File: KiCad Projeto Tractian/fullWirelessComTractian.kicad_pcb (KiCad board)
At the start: 4 copper layers, 23 parts, among them U1 ESP8266EX, U2 MX25R3235FM2xx1, U4 MX25R3235FM2xx1, U5 AMS1117-3.3, Y2 XTAL

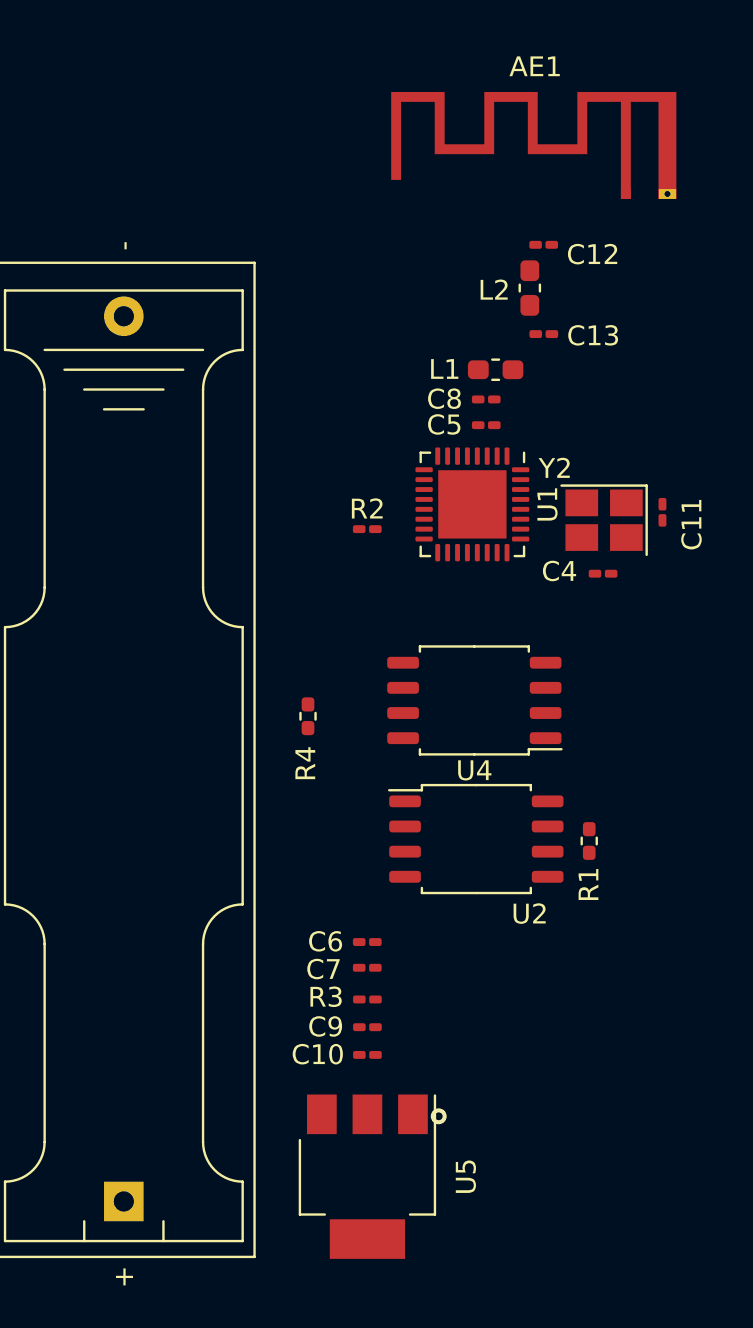
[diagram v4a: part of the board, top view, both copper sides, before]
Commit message: :construction: Schematics reorganizado | definicao de trail mils para power/GND lines e signal lines
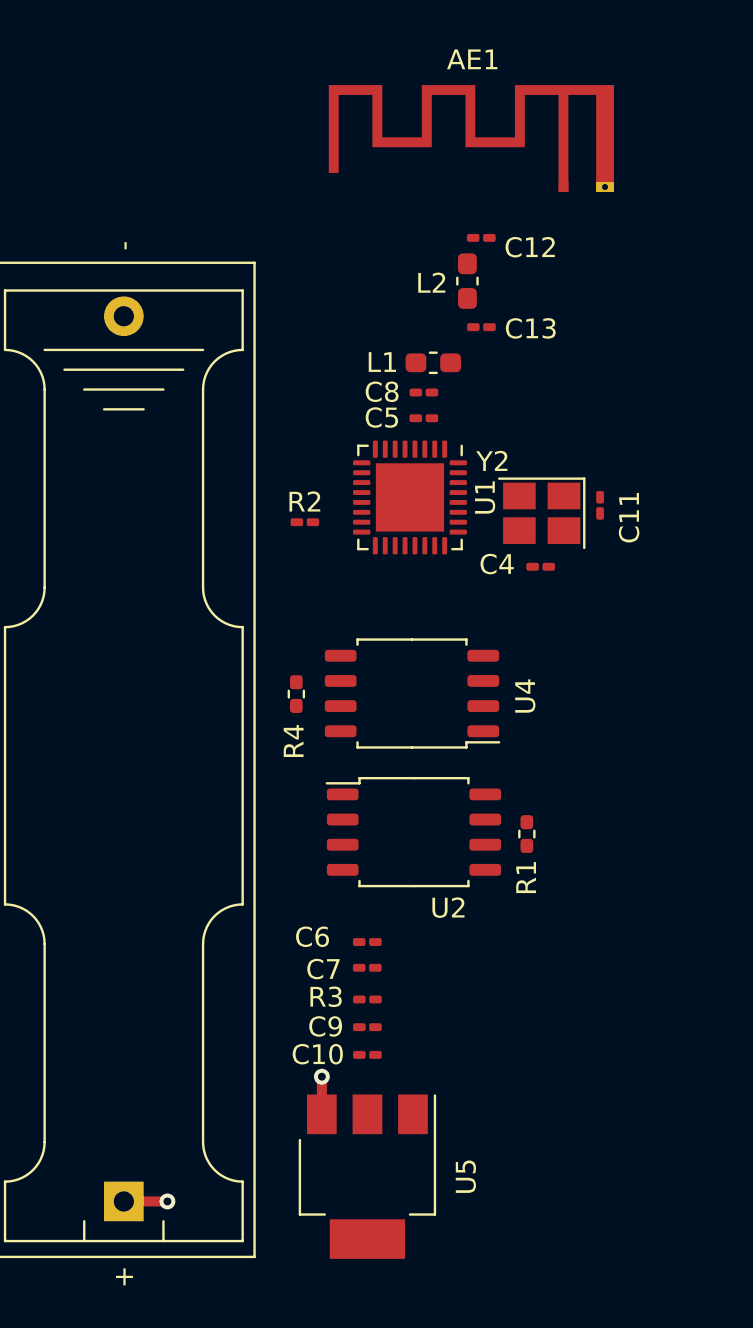
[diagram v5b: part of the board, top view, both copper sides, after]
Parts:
- Y2: value XTAL -> XTAL 16Mhz ±10ppm (TSX -3225 )
- moved AE1 3.17 mm to (149.5, 68.0)
- moved C11 3.17 mm to (151.3, 84.0)
- moved C13 3.17 mm to (145.4, 75.0)
- moved C8 3.17 mm to (142.4, 78.3)
- moved L2 3.17 mm to (144.7, 72.7)
- moved R1 3.17 mm to (147.7, 100.6)
- moved U2 3.17 mm to (141.9, 100.5)
- moved U4 3.17 mm to (141.8, 93.5)
- moved C12 3.17 mm to (145.3, 70.5)
- moved C4 3.17 mm to (148.3, 87.2)
- moved C5 3.17 mm to (142.4, 79.7)
- moved R2 3.17 mm to (136.4, 84.9)
- moved U1 3.17 mm to (141.8, 83.7)
- moved Y2 3.17 mm to (148.4, 84.5)
- moved L1 3.17 mm to (142.9, 76.8)
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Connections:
- net Net-(U1-VDDD) renamed VDD33
- net Net-(U2-SCLK) renamed DMSCK
- U1 pad 12: Net-(U1-MTCK) -> unconnected-(U1-MTCK-Pad12)
- U1 pad 14: Net-(U1-GPIO2) -> DMH
- U1 pad 15: Net-(U1-GPIO0) -> DMW
- U2 pad 3: Net-(U1-GPIO0) -> DMWP
- U2 pad 5: Net-(U1-MTCK) -> DMSI
- U2 pad 7: Net-(U1-GPIO2) -> DMHD
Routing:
- net Net-(BT1-+): track 0.00 -> 14.5 mm, vias 0 -> 2
- net (no net): vias 1 -> 0

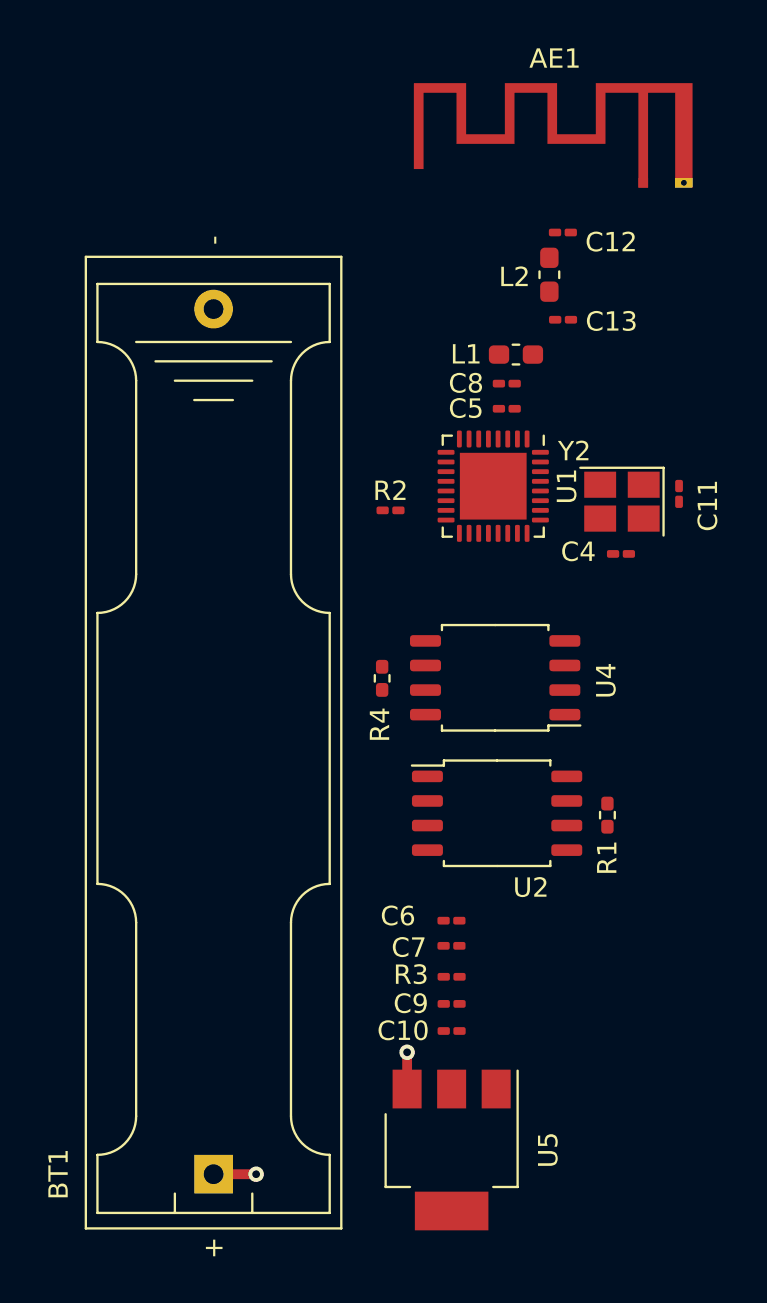
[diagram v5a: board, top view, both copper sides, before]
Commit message: 1 - :boom: | 2 - :memo: | 1- Calculo e projeto da impedancia de 50ohms para a antena RF | 2 - add datasheet antena RTexasSWRA117D 2.4GHz
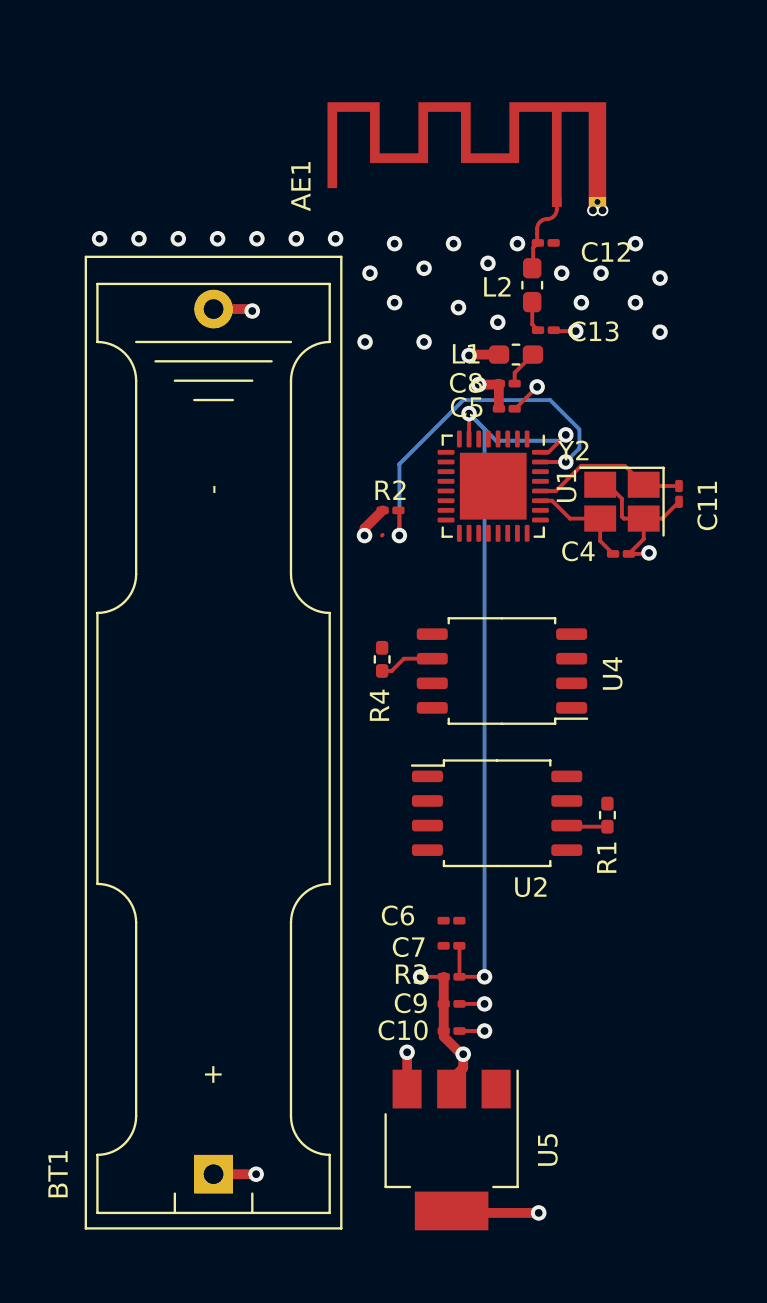
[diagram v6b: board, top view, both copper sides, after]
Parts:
- moved AE1 4.57 mm to (145.0, 69.0)
- moved C13 1.04 mm to (144.5, 75.6)
- moved L2 1.04 mm to (143.8, 73.3)
- moved C12 1.04 mm to (144.5, 71.1)
- moved R4 0.98 mm to (136.0, 92.6)
- moved U4 0.49 mm to (142.2, 93.2)
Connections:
- net DMSCK renamed DMCLK
- net Net-(U1-MTDI) renamed DMSO
- net Net-(U1-MTDO) renamed DMCS
- net Net-(U1-SDIO_CMD) renamed PMCS
- net Net-(U1-SDIO_DATA_0) renamed PMSO
- net Net-(U1-SDIO_DATA_1) renamed PMSI
- net Net-(U1-SDIO_DATA_2) renamed PMHD
- net Net-(U1-SDIO_DATA_3) renamed PMWP
- net Net-(U4-SCLK) renamed PMCLK
- U1 pad 12: unconnected-(U1-MTCK-Pad12) -> DMSI
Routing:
- net VDD33: track 0.00 -> 62.6 mm, vias 0 -> 5
- net Net-(U1-CHIP_PU): track 0.00 -> 41.0 mm, vias 0 -> 3
- net GND: track 0.00 -> 27.6 mm, vias 0 -> 34
- net Net-(U1-RES12K): track 0.00 -> 19.6 mm, vias 0 -> 2
- net Net-(U1-XTAL_IN): track 0.00 -> 8.13 mm
- net Net-(U1-XTAL_OUT): track 0.00 -> 5.57 mm
- net PMCLK: track 0.00 -> 2.85 mm
- net DMCLK: track 0.00 -> 2.12 mm
- net Net-(C8-Pad1): track 0.00 -> 1.89 mm
- net Net-(U1-LNA): track 0.00 -> 1.60 mm
- net Net-(AE1-A): track 0.00 -> 1.43 mm
- added copper zone on In1.Cu, net GND

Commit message: :construction: Nova organizacao da PCB | Routing in progress
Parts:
- added C1: 0.1uF, Capacitor_SMD:C_0201_0603Metric_Pad0.64x0.40mm_HandSolder, F.Cu at (151.4, 113.3)
- added C2: 2.2uF, Capacitor_Tantalum_SMD:CP_EIA-1608-08_AVX-J_Pad1.25x1.05mm_HandSolder, F.Cu at (151.4, 115.3)
- added R5: 220kΩ ±1%, Resistor_SMD:R_0201_0603Metric_Pad0.64x0.40mm_HandSolder, F.Cu at (152.3, 90.7)
- added R6: 100kΩ ±1%, Resistor_SMD:R_0201_0603Metric_Pad0.64x0.40mm_HandSolder, F.Cu at (152.3, 89.7)
- added U6: TMP36xS, Package_SO:SOIC-8_3.9x4.9mm_P1.27mm, F.Cu at (151.2, 109.9)
- moved AE1 34.4 mm to (160.3, 99.8), turned to -90 degrees
- moved C12 31.3 mm to (158.2, 99.2), turned to -90 degrees
- moved L2 28.1 mm to (156.0, 98.5), turned to 180 degrees
- moved C13 25.4 mm to (153.7, 99.2), turned to -90 degrees
- moved U2 22.2 mm to (148.5, 79.3), turned to 180 degrees
- moved L1 21.8 mm to (154.3, 95.4), turned to -90 degrees
- moved R1 21.5 mm to (142.3, 79.9), turned to 90 degrees
- moved C11 19.8 mm to (146.2, 103.2), turned to 180 degrees
- moved C8 19.6 mm to (152.8, 95.0), turned to 90 degrees
- moved R2 18.0 mm to (148.9, 97.9), turned to -90 degrees
- moved C5 17.8 mm to (151.5, 95.0), turned to 90 degrees
- moved Y2 16.0 mm to (145.8, 100.3), turned to 90 degrees
- moved C4 14.1 mm to (143.2, 100.3), turned to -90 degrees
- moved U1 11.8 mm to (147.7, 93.8), turned to 180 degrees
- moved R4 8.16 mm to (138.3, 100.4), turned to 180 degrees
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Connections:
- U1 pad 24: unconnected-(U1-GPIO5-Pad24) -> TMPSD
- U1 pad 6: unconnected-(U1-TOUT-Pad6) -> TOUT
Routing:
- net GND: track 27.6 -> 162.2 mm, vias 34 -> 24
- net VDD33: track 62.6 -> 136.4 mm, vias 5 -> 12
- net Net-(U1-CHIP_PU): track 41.0 -> 0.00 mm, vias 3 -> 0
- net PMSO: track 0.00 -> 23.3 mm
- net Net-(U1-RES12K): track 19.6 -> 0.00 mm, vias 2 -> 0
- net PMSI: track 0.00 -> 18.4 mm
- net Net-(U1-SDIO_CLK): track 0.00 -> 10.2 mm
- net PMWP: track 0.00 -> 10.0 mm
- net PMHD: track 0.00 -> 9.02 mm, vias 0 -> 2
- net PMCS: track 0.00 -> 6.22 mm
- net Net-(BT1-+): track 14.5 -> 11.8 mm, vias 2 -> 0
- net DMCLK: track 2.12 -> 0.00 mm
- net Net-(C8-Pad1): track 1.89 -> 0.00 mm
- net Net-(U1-LNA): track 1.60 -> 0.00 mm
- net Net-(AE1-A): track 1.43 -> 0.00 mm
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- removed copper zone on In1.Cu, net GND

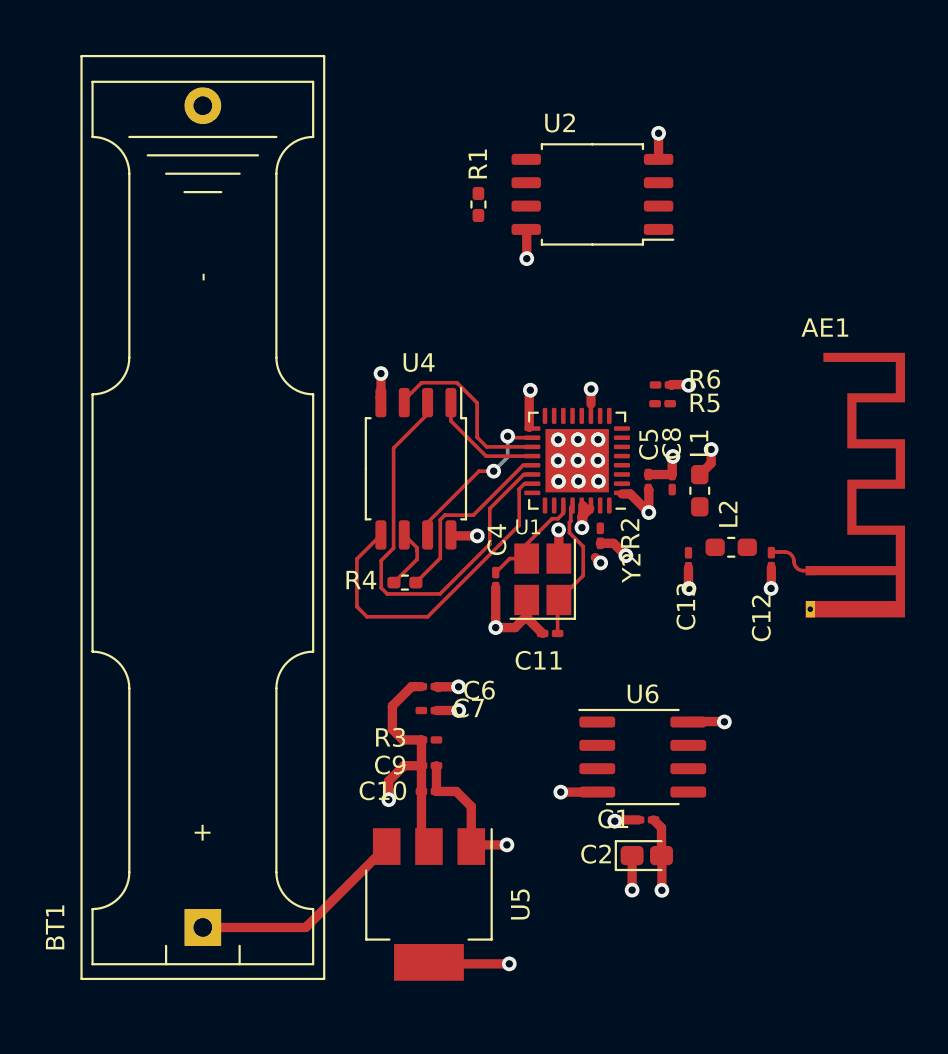
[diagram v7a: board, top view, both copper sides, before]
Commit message: :construction: PCB Routes Finished | PCB Borders defined | ANT1 track drawn manually (error ignore on no net connection for ANT1)
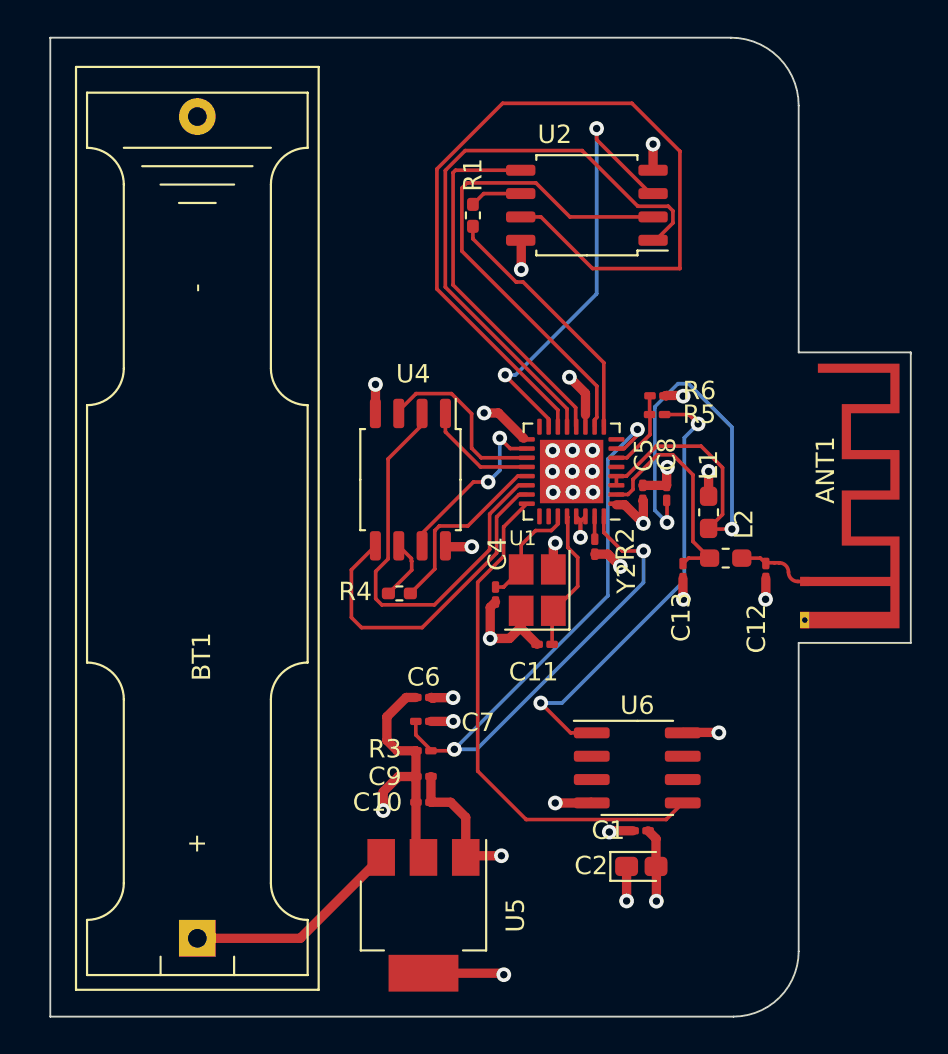
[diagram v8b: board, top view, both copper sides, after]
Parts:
- moved L1 1.27 mm to (154.8, 96.6)
- moved C4 0.78 mm to (143.2, 101.1)
- moved C11 0.66 mm to (145.9, 103.8)
- moved C12 0.66 mm to (157.9, 99.8)
- moved C5 0.66 mm to (151.2, 95.6)
- moved C6 0.66 mm to (139.3, 106.7)
- moved C8 0.66 mm to (152.5, 95.6)
- moved R5 0.66 mm to (152.0, 91.3)
- moved R6 0.66 mm to (152.0, 90.3)
- moved U2 0.66 mm to (148.2, 79.9)
- moved BT1 0.66 mm to (127.0, 119.8)
- moved ANT1 0.66 mm to (160.0, 100.4)
- moved C13 0.66 mm to (153.4, 99.8)
- moved C7 0.66 mm to (139.3, 108.0)
- moved C1 0.66 mm to (151.1, 113.9)
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- renumbered AE1 to ANT1
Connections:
- U1 pad 14: DMH -> DMHD
- U1 pad 15: DMW -> DMWP
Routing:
- net DMHD: track 0.00 -> 48.7 mm
- net Net-(U1-CHIP_PU): track 0.00 -> 45.8 mm, vias 0 -> 3
- net DMCS: track 0.00 -> 33.0 mm
- net Net-(C8-Pad1): track 0.00 -> 31.3 mm, vias 0 -> 2
- net TMPSD: track 0.00 -> 28.3 mm
- net DMSO: track 0.00 -> 27.4 mm
- net Net-(U6-V_{OUT}): track 0.00 -> 24.9 mm, vias 0 -> 2
- net DMWP: track 0.00 -> 24.3 mm, vias 0 -> 2
- net DMSI: track 0.00 -> 20.3 mm
- net Net-(U1-MTMS): track 0.00 -> 14.1 mm
- net Net-(U1-LNA): track 0.00 -> 12.3 mm
- net TOUT: track 0.00 -> 4.47 mm
- net DMCLK: track 0.00 -> 2.84 mm
- net VDD33: track 136.4 -> 138.5 mm
- net Net-(ANT1-A): track 0.00 -> 1.43 mm
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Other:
- board outline added: 46.8 x 53.3 mm
